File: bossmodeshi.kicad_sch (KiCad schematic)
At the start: 48 parts, among them Q1 M_CHG, Q2 M_DSG, Q4 NPN_REGIN, U1 MP2790DFP-0000-T

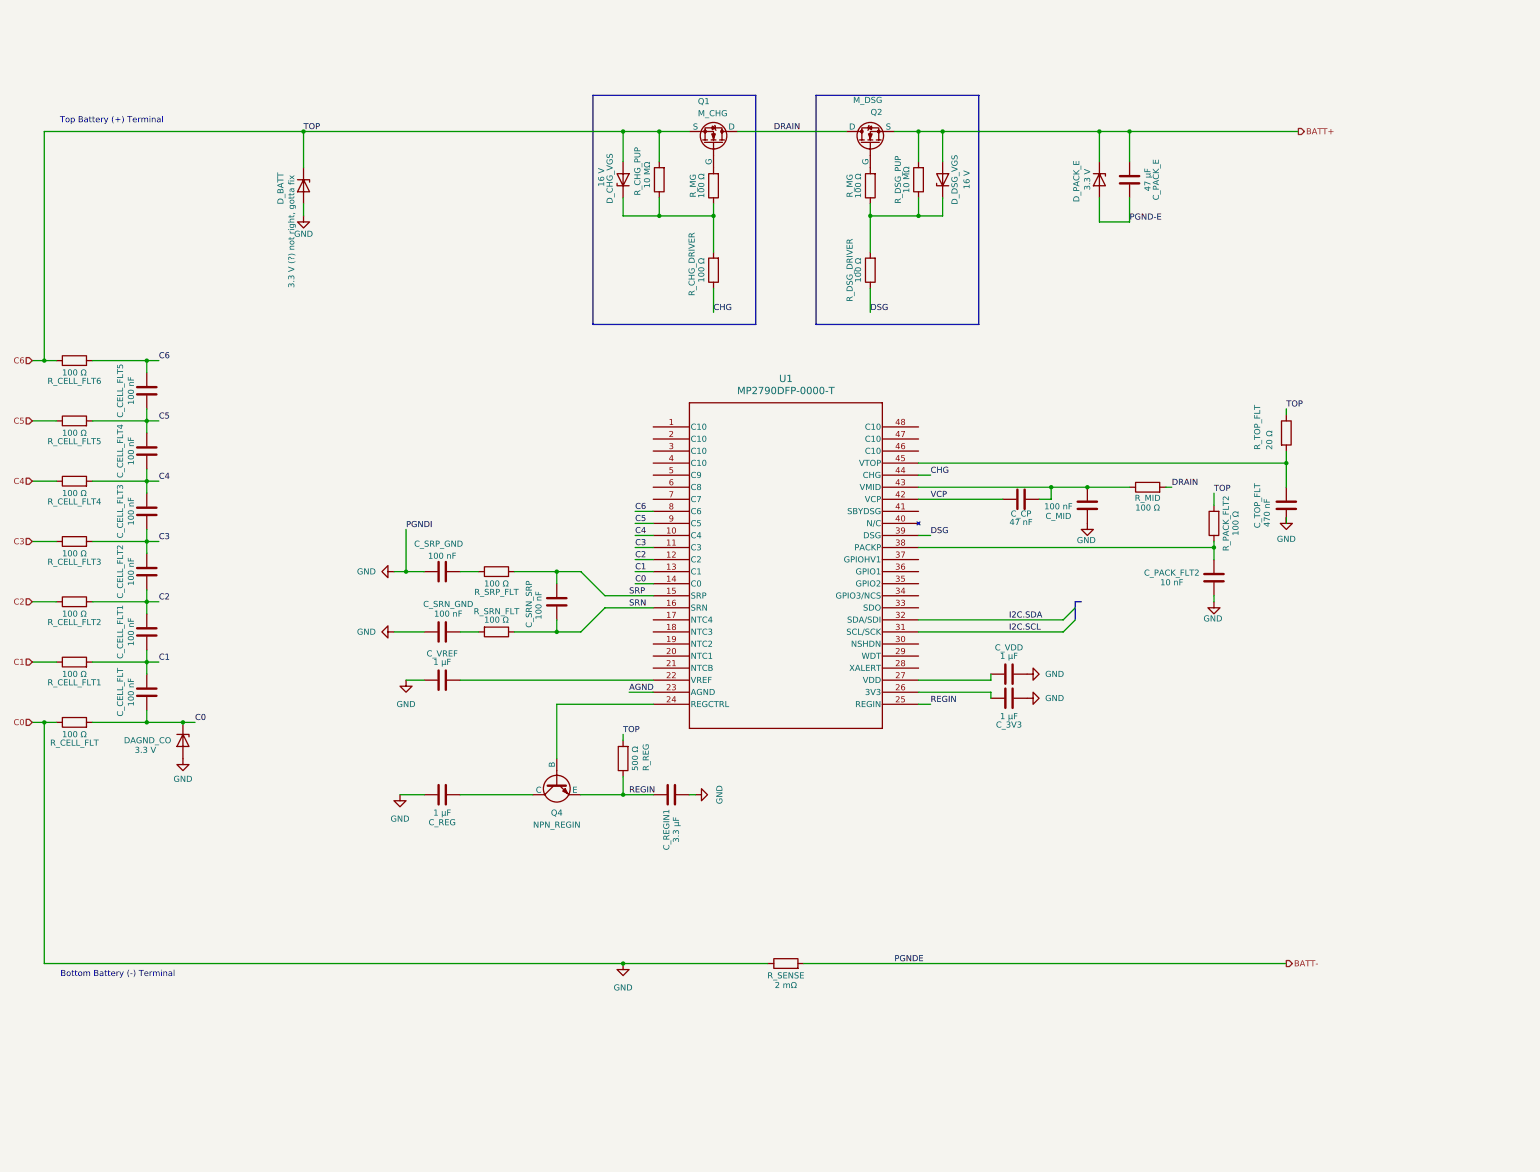
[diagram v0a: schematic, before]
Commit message: Fixing and cleaning up schematic
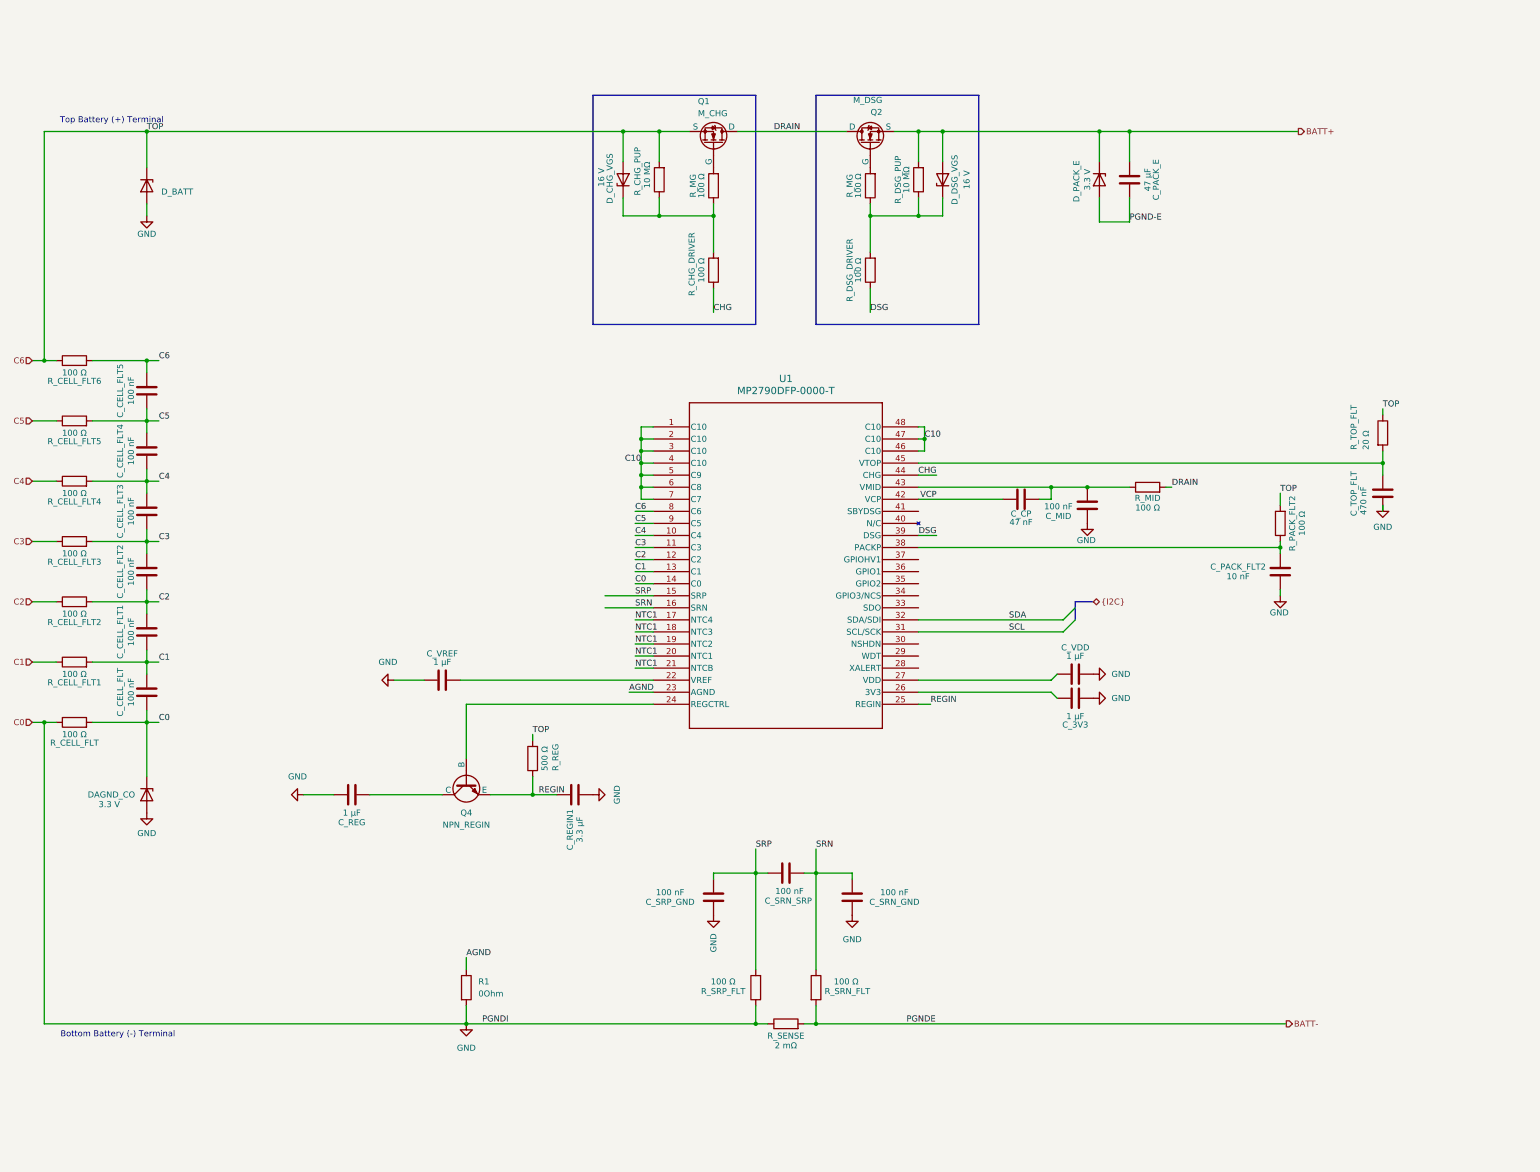
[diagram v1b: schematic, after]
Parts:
- added R1: 0Ohm, symbol Device:R
- C_REG, C_VREF: footprint (none) -> Capacitor_SMD:C_0805_2012Metric
- C_REGIN1: footprint (none) -> Capacitor_SMD:C_1210_3225Metric
- C_SRN_GND, C_SRN_SRP, C_SRP_GND: footprint (none) -> Capacitor_SMD:C_1206_3216Metric
- D_BATT: value 3.3 V (?) not right, gotta fix -> (none)
- R_REG, R_SRN_FLT, R_SRP_FLT: footprint (none) -> Resistor_SMD:R_0603_1608Metric
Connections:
- net AGND: now also R1.1
- net BATT-: now also R_SRN_FLT.2
- net GND: now also C_SRP_GND.2, R_SRP_FLT.1, R1.2; no longer C_SRP_GND.1
- net SRN: now also C_SRN_GND.2
- net SRP: now also C_SRP_GND.1
- net C10: now reaches U1.1 (C10)
- net C10: now also U1.2 (C10), U1.3 (C10), U1.4 (C10), U1.46 (C10), U1.47 (C10), U1.48 (C10), U1.5 (C9), U1.6 (C8), U1.7 (C7)
- net NTC1: now reaches U1.17 (NTC4)
- net NTC1: now also U1.18 (NTC3), U1.19 (NTC2), U1.20 (NTC1), U1.21 (NTCB)
- net I2C.SCL renamed SCL
- net I2C.SDA renamed SDA
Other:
- moved on the sheet: C_3V3, C_PACK_FLT2, C_REG, C_REGIN1, C_SRN_GND, C_SRN_SRP, C_SRP_GND, C_TOP_FLT, C_VDD, DAGND_CO, D_BATT, Q4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

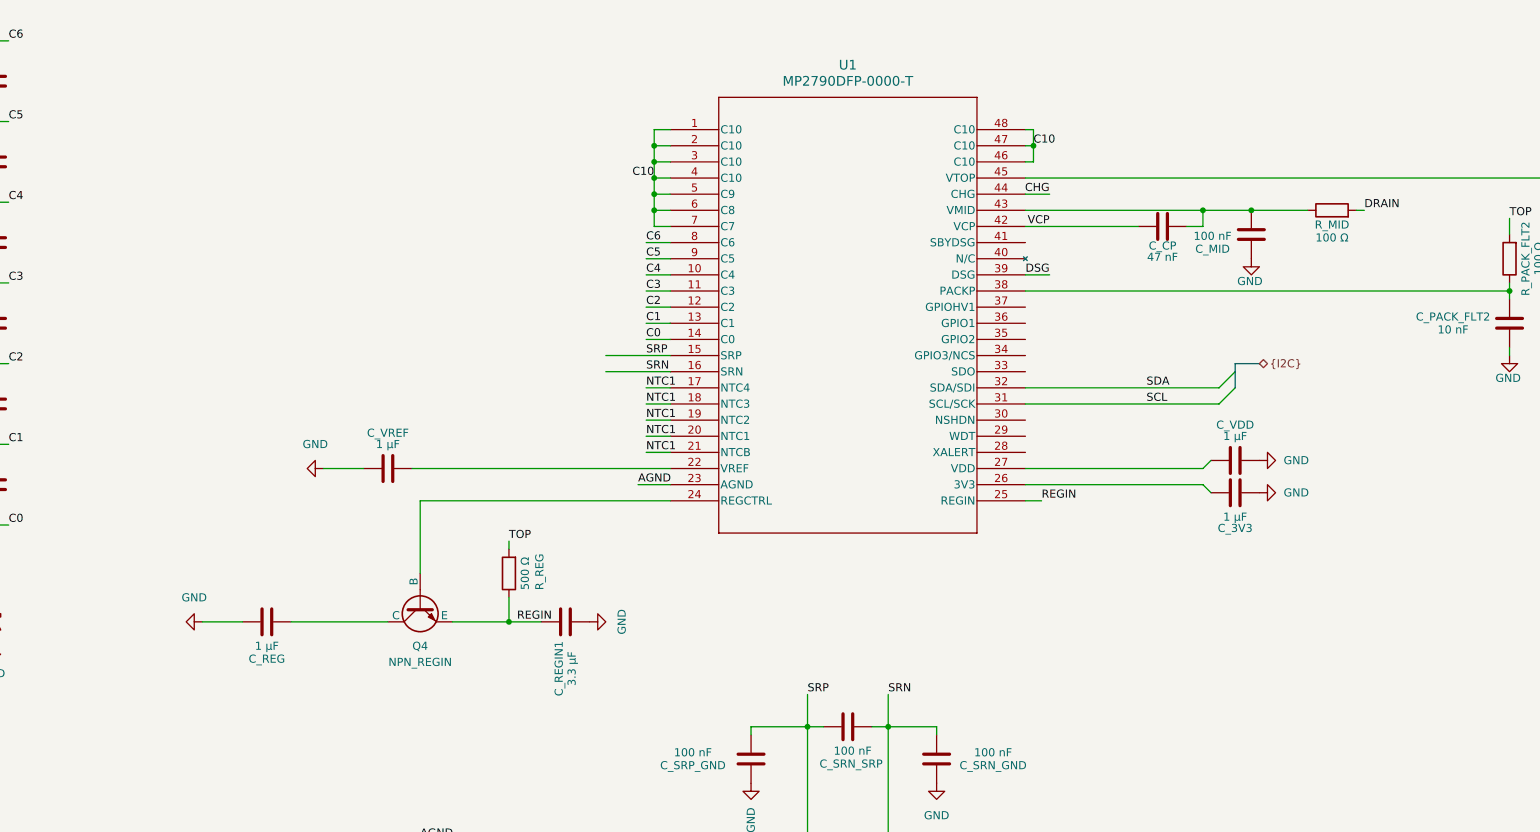
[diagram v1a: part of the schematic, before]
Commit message: Reviewed and cleaned up schematic
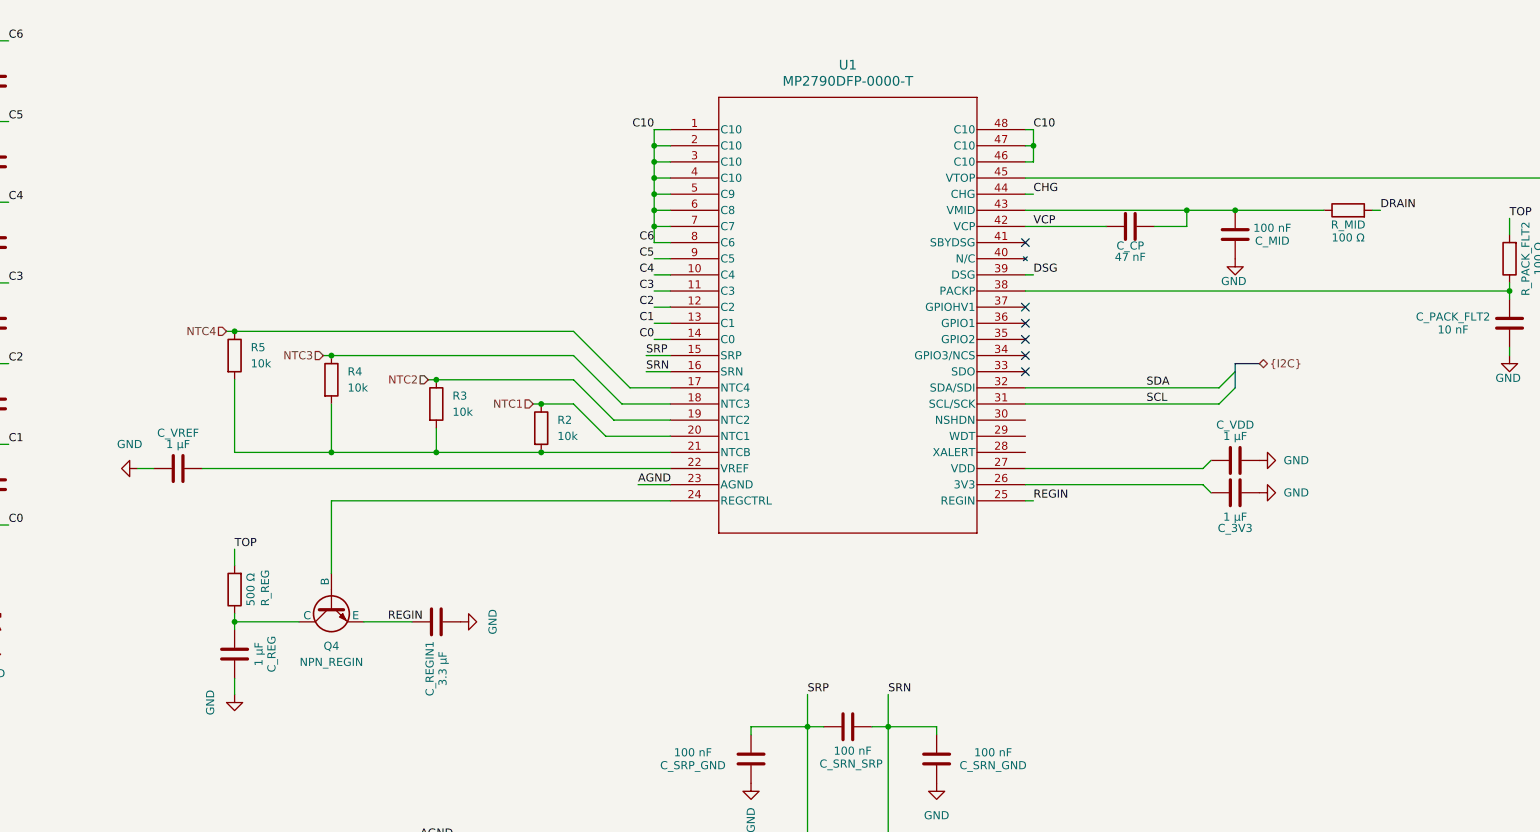
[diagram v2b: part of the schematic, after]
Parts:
- added R2, R3, R4, R5: 10k, symbol Device:R
- D_BATT: value (none) -> ~
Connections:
- net C10 is gone; now on net C6: U1.1 (C10), U1.2 (C10), U1.3 (C10), U1.4 (C10), U1.46 (C10), U1.47 (C10), U1.48 (C10), U1.5 (C9), U1.6 (C8), U1.7 (C7)
- net NTC1: now also R2.1; no longer U1.17 (NTC4), U1.18 (NTC3), U1.19 (NTC2), U1.21 (NTCB)
- net REGIN: no longer R_REG.1
- net at C_REG.1, Q4.1 (C): now also R_REG.1
- new net: R2.2, R3.2, R4.2, R5.2, U1.21 (NTCB)
- new net NTC2: R3.1, U1.19 (NTC2)
- new net NTC3: R4.1, U1.18 (NTC3)
- new net NTC4: R5.1, U1.17 (NTC4)
- no-connect marks 0 -> 6
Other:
- moved on the sheet: C_CP, C_MID, C_REG, C_REGIN1, C_VREF, Q4, R_MID, R_REG

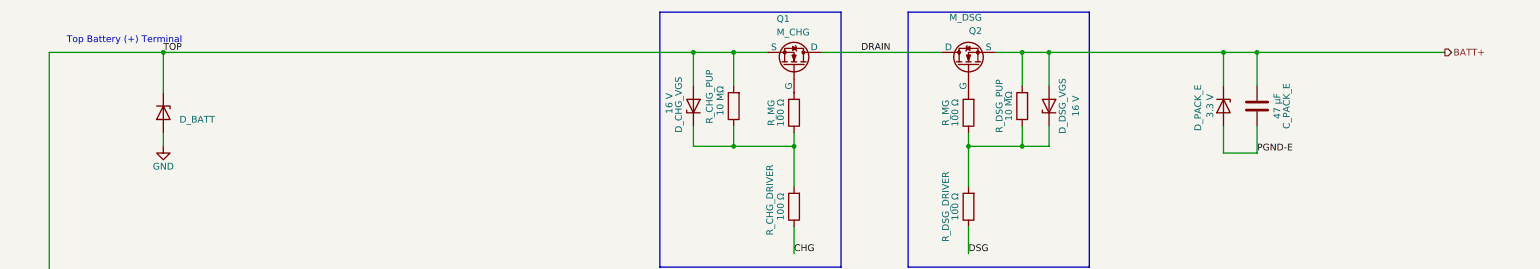
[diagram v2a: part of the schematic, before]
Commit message: Finishing gate drive stuff
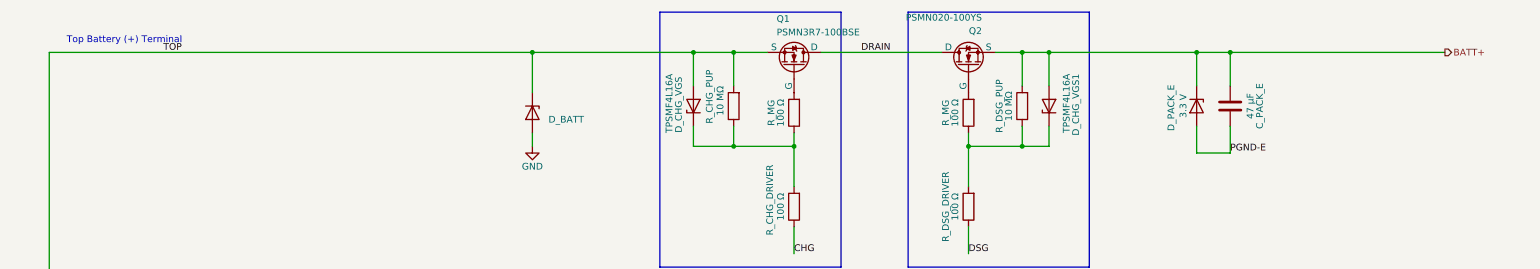
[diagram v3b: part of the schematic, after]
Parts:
- removed D_DSG_VGS: 16 V, symbol Device:D_Zener
- added D_CHG_VGS1: TPSMF4L16A, Diode_SMD:Nexperia_CFP3_SOD-123W, symbol Device:D_Zener
- D_CHG_VGS: value 16 V -> TPSMF4L16A; footprint (none) -> Diode_SMD:Nexperia_CFP3_SOD-123W; MFR (none) -> Littelfuse Inc.; MFR P/N (none) -> TPSMF4L16A; Supplier_1 (none) -> Digikey; Supplier_1 P/N (none) -> F7539TR-ND; Supplier_1 Price @ QTY (none) -> 1; Supplier_1 Unit Price (none) -> 0.15000
- Q1: value M_CHG -> PSMN3R7-100BSE; footprint (none) -> Package_TO_SOT_SMD:TO-263-2; MFR (none) -> Nexperia USA Inc.; MFR P/N (none) -> PSMN3R7-100BSEJ; Supplier_1 (none) -> Digikey; Supplier_1 P/N (none) -> 1727-PSMN3R7-100BSEJTR-ND; Supplier_1 Price @ QTY (none) -> 1; Supplier_1 Unit Price (none) -> 6.51
- Q2: value M_DSG -> PSMN020-100YS; footprint (none) -> Package_TO_SOT_SMD:LFPAK56; MFR (none) -> Nexperia USA Inc.; MFR P/N (none) -> PSMN020-100YS,115; Supplier_1 (none) -> Digikey; Supplier_1 P/N (none) -> 1727-4286-2-ND; Supplier_1 Price @ QTY (none) -> 1; Supplier_1 Unit Price (none) -> 2.09000
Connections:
- net BATT+: now also D_CHG_VGS1.2 (A)
- net at R_DSG_DRIVER.2, R_DSG_PUP.1, R_MG.1: now also D_CHG_VGS1.1 (K)
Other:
- moved on the sheet: C_PACK_E, D_BATT, D_PACK_E

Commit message: added resistors for thermistors
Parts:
- R2, R3, R4, R5: Mfr (none) -> Panasonic Electronic Components; Mfr P/N (none) -> ERA-3AEB103V; Supplier_1 (none) -> DigiKey; Supplier_1 P/N (none) -> P10KDBTR-ND; Supplier_1 Price @ Qty (none) -> 1; Supplier_1 Unit Price (none) -> 0.10

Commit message: Pushing
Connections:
- net C1: no longer C_CELL_FLT.2, C_CELL_FLT1.1, R_CELL_FLT1.2, U1.13 (C1)
- net C2: no longer C_CELL_FLT1.2, C_CELL_FLT2.1, R_CELL_FLT2.2, U1.12 (C2)
- net C3: no longer C_CELL_FLT2.2, C_CELL_FLT3.1, R_CELL_FLT3.2, U1.11 (C3)
- net C4: no longer C_CELL_FLT3.2, C_CELL_FLT4.1, R_CELL_FLT4.2, U1.10 (C4)
- net C5: no longer C_CELL_FLT4.2, C_CELL_FLT5.1, R_CELL_FLT5.2, U1.9 (C5)
- net C6: no longer C_CELL_FLT5.2, R_CELL_FLT6.2, U1.1 (C10), U1.2 (C10), U1.3 (C10), U1.4 (C10), U1.46 (C10), U1.47 (C10), U1.48 (C10), U1.5 (C9), U1.6 (C8), U1.7 (C7), U1.8 (C6)
- net GND: no longer C_CELL_FLT.1, DAGND_CO.1 (K), R_CELL_FLT.2, U1.14 (C0)
- new net C10: U1.46 (C10), U1.47 (C10), U1.48 (C10)
- new net CELL_0: C_CELL_FLT.1, DAGND_CO.1 (K), R_CELL_FLT.2
- new net CELL_1: C_CELL_FLT.2, C_CELL_FLT1.1, R_CELL_FLT1.2
- new net CELL_2: C_CELL_FLT1.2, C_CELL_FLT2.1, R_CELL_FLT2.2
- new net CELL_3: C_CELL_FLT2.2, C_CELL_FLT3.1, R_CELL_FLT3.2, U1.11 (C3)
- new net CELL_4: C_CELL_FLT3.2, C_CELL_FLT4.1, R_CELL_FLT4.2, U1.10 (C4)
- new net CELL_5: C_CELL_FLT4.2, C_CELL_FLT5.1, R_CELL_FLT5.2, U1.9 (C5)
- new net CELL_6: C_CELL_FLT5.2, R_CELL_FLT6.2, U1.1 (C10), U1.2 (C10), U1.3 (C10), U1.4 (C10), U1.5 (C9), U1.6 (C8), U1.7 (C7), U1.8 (C6)
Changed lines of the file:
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@@
 		)
 	)
-	(label "C2"
+	(label "CELL_2"
 		(at 73.66 147.32 0)
 		(effects
@@
 		)
 	)
-	(label "C4"
+	(label "CELL_4"
 		(at 73.66 121.92 0)
 		(effects
@@
 		)
 	)
-	(label "C0"
-		(at 175.26 143.51 180)
-		(effects
-			(font
-				(size 1.27 1.27)
-			)
-			(justify right bottom)
-		)
-	)
-	(label "C6"
-		(at 175.26 128.27 180)
-		(effects
-			(font
-				(size 1.27 1.27)
-			)
-			(justify right bottom)
-		)
-	)
-	(label "C1"
-		(at 175.26 140.97 180)
+	(label "CELL_5"
+		(at 175.26 130.81 180)
 		(effects
 			(font
@@
 		)
 	)
-	(label "C10"
-		(at 175.26 110.49 180)
-		(effects
-			(font
-				(size 1.27 1.27)
-			)
-			(justify right bottom)
-		)
-	)
-	(label "C3"
+	(label "CELL_3"
 		(at 73.66 134.62 0)
 		(effects
@@
 		)
 	)
-	(label "C6"
+	(label "CELL_6"
 		(at 73.66 96.52 0)
 		(effects
@@
 		)
 	)
+	(label "CELL_6"
+		(at 175.26 128.27 180)
+		(effects
+			(font
+				(size 1.27 1.27)
+			)
+			(justify right bottom)
+		)
+	)
 	(label "PGNDE"
 		(at 231.14 236.22 0)
@@
 		)
 	)
-	(label "C0"
+	(label "CELL_0"
 		(at 73.66 172.72 0)
 		(effects
@@
 		)
 	)
-	(label "C3"
-		(at 175.26 135.89 180)
+	(label "CELL_4"
+		(at 175.26 133.35 180)
 		(effects
 			(font
@@
 		)
 	)
-	(label "C5"
-		(at 175.26 130.81 180)
+	(label "CELL_3"
+		(at 175.26 135.89 180)
 		(effects
 			(font
@@
 		)
 	)
-	(label "C5"
+	(label "CELL_5"
 		(at 73.66 109.22 0)
 		(effects
@@
 		)
 	)
-	(label "C4"
-		(at 175.26 133.35 180)
-		(effects
-			(font
-				(size 1.27 1.27)
-			)
-			(justify right bottom)
-		)
-	)
-	(label "C1"
+	(label "CELL_1"
 		(at 73.66 160.02 0)
 		(effects
@@
 		)
 	)
-	(label "C2"
-		(at 175.26 138.43 180)
-		(effects
-			(font
-				(size 1.27 1.27)
-			)
-			(justify right bottom)
-		)
-	)

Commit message: small changes, nothing crazy
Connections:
- net CELL_0: now also U1.14 (C0)
- net CELL_1: now also U1.13 (C1)
- net CELL_2: now also U1.12 (C2)
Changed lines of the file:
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@@
 	(text "Top Battery (+) Terminal"
 		(exclude_from_sim no)
-		(at 63.754 45.974 0)
+		(at 61.976 46.736 0)
 		(effects
 			(font
@@
 		)
 	)
+	(label "CELL_1"
+		(at 175.26 140.97 180)
+		(effects
+			(font
+				(size 1.27 1.27)
+			)
+			(justify right bottom)
+		)
+	)
 	(label "CELL_5"
 		(at 175.26 130.81 180)
@@
 	)
 	(label "TOP"
-		(at 71.12 48.26 0)
+		(at 78.74 48.26 0)
 		(effects
 			(font
@@
 		)
 	)
+	(label "CELL_0"
+		(at 175.26 143.51 180)
+		(effects
+			(font
+				(size 1.27 1.27)
+			)
+			(justify right bottom)
+		)
+	)
 	(label "SRP"
 		(at 173.99 146.05 0)
@@
 		)
 	)
+	(label "CELL_2"
+		(at 175.26 138.43 180)
+		(effects
+			(font
+				(size 1.27 1.27)
+			)
+			(justify right bottom)
+		)
+	)
 	(label "CELL_3"
 		(at 175.26 135.89 180)
@@
 		(dnp no)
 		(property "Reference" "R_CELL_FLT6"
-			(at 55.88 100.838 90)
+			(at 55.88 98.552 90)
 			(effects
 				(font
@@
 		)
 		(property "Value" "100 Ω"
-			(at 55.88 99.06 90)
+			(at 55.88 100.33 90)
 			(effects
 				(font
